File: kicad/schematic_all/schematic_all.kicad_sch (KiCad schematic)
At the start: 40 parts, among them J1 Power In, SW1 Button 1, SW2 Encoder 1, SW3 Button 2, SW4 Encoder 2, SW5 Button 3, U1 L7805, U2 RPi_Pico, U3 RDA5807M_Module, U4 LM386

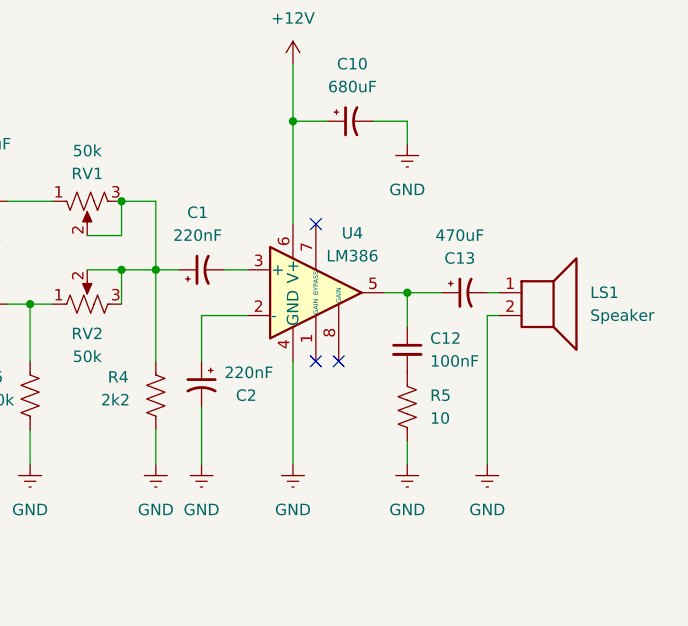
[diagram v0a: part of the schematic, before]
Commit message: Minor changes & Added additional testpoints
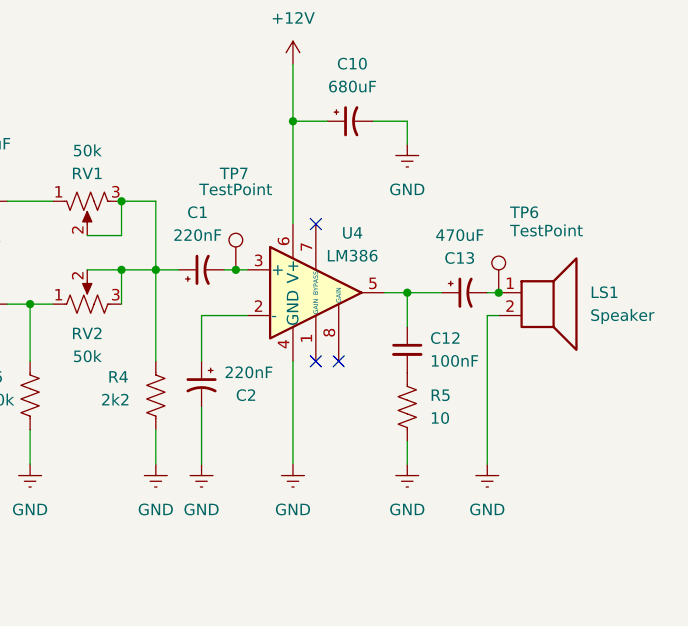
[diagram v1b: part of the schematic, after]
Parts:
- added TP6, TP7: TestPoint, Connector_PinHeader_2.54mm:PinHeader_1x01_P2.54mm_Vertical, symbol Connector:TestPoint
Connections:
- net at C1.2, U4.3 (+): now also TP7.1
- net at C13.2, LS1.1: now also TP6.1
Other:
- company: (none) -> Thomas Cool & Andrew Fischer
- title: (none) -> ECE 299 - Alarm Clock Radio
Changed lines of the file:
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@@
 	(generator_version "8.0")
 	(paper "A4")
+	(title_block
+		(title "ECE 299 - Alarm Clock Radio")
+		(date "2024-05-21")
+		(rev "6")
+		(company "Thomas Cool & Andrew Fischer")
+	)
 	(junction
 		(at 31.75 72.39)
@@
 	)
 	(junction
+		(at 261.62 129.54)
+		(diameter 0)
+		(color 0 0 0 0)
+	)
+	(junction
 		(at 77.47 63.5)
 		(diameter 0)
@@
 		(color 0 0 0 0)
 	)
+	(junction
+		(at 232.41 127)
+		(diameter 0)
+		(color 0 0 0 0)
+	)
 	(no_connect
 		(at 132.08 86.36)
@@
 	(wire
 		(pts
-			(xy 231.14 127) (xy 233.68 127)
+			(xy 231.14 127) (xy 232.41 127)
 		)
 		(stroke
@@
 	(wire
 		(pts
+			(xy 260.35 132.08) (xy 260.35 148.59)
+		)
+		(stroke
+			(width 0)
+			(type default)
+		)
+	)
+	(wire
+		(pts
 			(xy 41.91 69.85) (xy 41.91 72.39)
 		)
@@
 	(wire
 		(pts
+			(xy 232.41 127) (xy 233.68 127)
+		)
+		(stroke
+			(width 0)
+			(type default)
+		)
+	)
+	(wire
+		(pts
 			(xy 53.34 119.38) (xy 59.69 119.38)
 		)
@@
 	(wire
 		(pts
-			(xy 260.35 148.59) (xy 260.35 132.08)
-		)
-		(stroke
-			(width 0)
-			(type default)
-		)
-	)
-	(wire
-		(pts
 			(xy 248.92 129.54) (xy 251.46 129.54)
 		)
@@
 	)
 	(symbol
+		(lib_id "Connector:TestPoint")
+		(at 261.62 129.54 0)
+		(unit 1)
+		(exclude_from_sim no)
+		(in_bom yes)
+		(on_board yes)
+		(dnp no)
+		(property "Reference" "TP6"
+			(at 262.89 120.65 0)
+			(effects
+				(font
+					(size 1.27 1.27)
+				)
+				(justify left)
+			)
+		)
+		(property "Value" "TestPoint"
+			(at 262.89 122.682 0)
+			(effects
+				(font
+					(size 1.27 1.27)
+				)
+				(justify left)
+			)
+		)
+		(property "Footprint" "Connector_PinHeader_2.54mm:PinHeader_1x01_P2.54mm_Vertical"
+			(at 266.7 129.54 0)
+			(effects
+				(font
+					(size 1.27 1.27)
+				)
+				(hide yes)
+			)
+		)
+		(property "Datasheet" "~"
+			(at 266.7 129.54 0)
+			(effects
+				(font
+					(size 1.27 1.27)
+				)
+				(hide yes)
+			)
+		)
+		(property "Description" "test point"
+			(at 261.62 129.54 0)
+			(effects
+				(font
+					(size 1.27 1.27)
+				)
+				(hide yes)
+			)
+		)
+		(pin "1"
+		)
+		(instances
+			(project "schematic_all"
+				(path "/017a32bd-a431-4565-87b4-2161296abf15"
+					(reference "TP6")
+					(unit 1)
+				)
+			)
+		)
+	)
+	(symbol
 		(lib_id "power:+12V")
 		(at 29.21 20.32 0)
@@
 					(unit 1)
 				)
+			)
+		)
+	)
+	(symbol
+		(lib_id "Connector:TestPoint")
+		(at 232.41 127 0)
+		(unit 1)
+		(exclude_from_sim no)
+		(in_bom yes)
+		(on_board yes)
+		(dnp no)
+		(property "Reference" "TP7"
+			(at 230.632 116.332 0)
+			(effects
+				(font
+					(size 1.27 1.27)
+				)
+				(justify left)
+			)
+		)
+		(property "Value" "TestPoint"
+			(at 228.346 118.11 0)
+			(effects
+				(font
+					(size 1.27 1.27)
+				)
+				(justify left)
+			)
+		)
+		(property "Footprint" "Connector_PinHeader_2.54mm:PinHeader_1x01_P2.54mm_Vertical"
+			(at 237.49 127 0)
+			(effects
+				(font
+					(size 1.27 1.27)
+				)
+				(hide yes)
+			)
+		)
+		(property "Datasheet" "~"
+			(at 237.49 127 0)
+			(effects
+				(font
+					(size 1.27 1.27)
+				)
+				(hide yes)
+			)
+		)
+		(property "Description" "test point"
+			(at 232.41 127 0)
+			(effects
+				(font
+					(size 1.27 1.27)
+				)
+				(hide yes)
+			)
+		)
+		(pin "1"
+		)
+		(instances
+			(project "schematic_all"
+				(path "/017a32bd-a431-4565-87b4-2161296abf15"
+					(reference "TP7")
+					(unit 1)
+				)

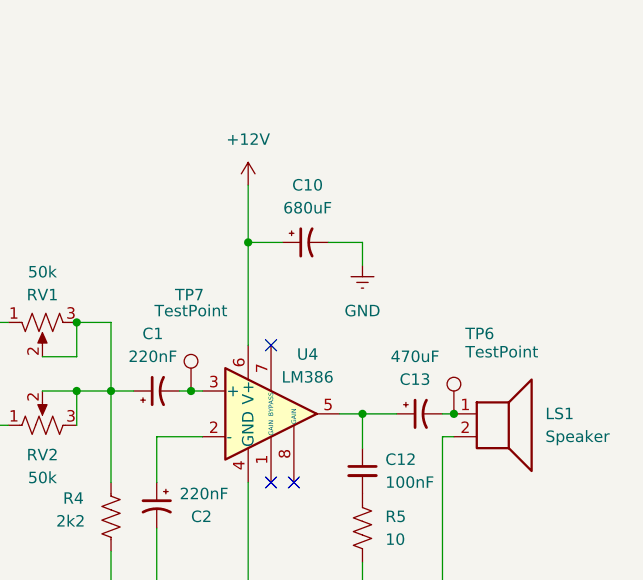
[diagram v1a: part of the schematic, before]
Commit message: adjustments on test points and ink
move speaker test point to before capacitor
increase size of designed by text
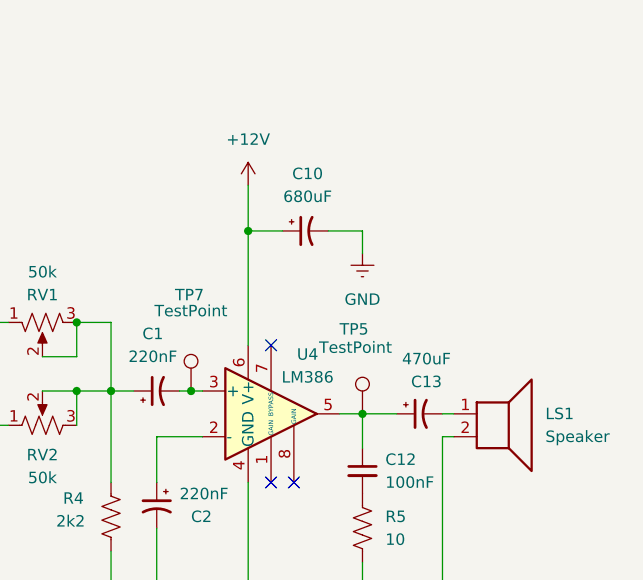
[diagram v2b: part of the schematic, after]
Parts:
- removed TP6: TestPoint, Connector_PinHeader_2.54mm:PinHeader_1x01_P2.54mm_Vertical, symbol Connector:TestPoint
- added TP5: TestPoint, Connector_PinHeader_2.54mm:PinHeader_1x01_P2.54mm_Vertical, symbol Connector:TestPoint
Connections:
- net at C12.1, C13.1, U4.5: now also TP5.1
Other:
- moved on the sheet: C10
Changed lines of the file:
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@@
 	)
 	(junction
-		(at 170.18 66.04)
+		(at 238.76 109.22)
 		(diameter 0)
 		(color 0 0 0 0)
 	)
 	(junction
-		(at 110.49 93.98)
+		(at 170.18 66.04)
 		(diameter 0)
 		(color 0 0 0 0)
 	)
 	(junction
-		(at 41.91 60.96)
+		(at 110.49 93.98)
 		(diameter 0)
 		(color 0 0 0 0)
 	)
 	(junction
-		(at 219.71 119.38)
+		(at 41.91 60.96)
 		(diameter 0)
 		(color 0 0 0 0)
 	)
 	(junction
-		(at 261.62 129.54)
+		(at 219.71 119.38)
 		(diameter 0)
 		(color 0 0 0 0)
@@
 	)
 	(junction
-		(at 238.76 110.49)
-		(diameter 0)
-		(color 0 0 0 0)
-	)
-	(junction
 		(at 120.65 93.98)
 		(diameter 0)
@@
 	(wire
 		(pts
-			(xy 251.46 110.49) (xy 251.46 113.03)
+			(xy 251.46 109.22) (xy 251.46 111.76)
 		)
 		(stroke
@@
 	(wire
 		(pts
-			(xy 247.65 110.49) (xy 251.46 110.49)
+			(xy 247.65 109.22) (xy 251.46 109.22)
 		)
 		(stroke
@@
 	(wire
 		(pts
-			(xy 238.76 110.49) (xy 242.57 110.49)
+			(xy 238.76 109.22) (xy 242.57 109.22)
 		)
 		(stroke
@@
 	(wire
 		(pts
-			(xy 238.76 110.49) (xy 238.76 121.92)
-		)
-		(stroke
-			(width 0)
-			(type default)
-		)
-	)
-	(wire
-		(pts
 			(xy 236.22 58.42) (xy 246.38 58.42)
 		)
@@
 	(wire
 		(pts
-			(xy 238.76 104.14) (xy 238.76 110.49)
+			(xy 238.76 104.14) (xy 238.76 109.22)
 		)
 		(stroke
@@
 	(wire
 		(pts
+			(xy 238.76 109.22) (xy 238.76 121.92)
+		)
+		(stroke
+			(width 0)
+			(type default)
+		)
+	)
+	(wire
+		(pts
 			(xy 86.36 121.92) (xy 86.36 111.76)
 		)
@@
 	)
 	(symbol
-		(lib_id "Connector:TestPoint")
-		(at 261.62 129.54 0)
-		(unit 1)
-		(exclude_from_sim no)
-		(in_bom yes)
-		(on_board yes)
-		(dnp no)
-		(property "Reference" "TP6"
-			(at 262.89 120.65 0)
-			(effects
-				(font
-					(size 1.27 1.27)
-				)
-				(justify left)
-			)
-		)
-		(property "Value" "TestPoint"
-			(at 262.89 122.682 0)
-			(effects
-				(font
-					(size 1.27 1.27)
-				)
-				(justify left)
-			)
-		)
-		(property "Footprint" "Connector_PinHeader_2.54mm:PinHeader_1x01_P2.54mm_Vertical"
-			(at 266.7 129.54 0)
-			(effects
-				(font
-					(size 1.27 1.27)
-				)
-				(hide yes)
-			)
-		)
-		(property "Datasheet" "~"
-			(at 266.7 129.54 0)
-			(effects
-				(font
-					(size 1.27 1.27)
-				)
-				(hide yes)
-			)
-		)
-		(property "Description" "test point"
-			(at 261.62 129.54 0)
-			(effects
-				(font
-					(size 1.27 1.27)
-				)
-				(hide yes)
-			)
-		)
-		(pin "1"
-		)
-		(instances
-			(project "schematic_all"
-				(path "/017a32bd-a431-4565-87b4-2161296abf15"
-					(reference "TP6")
-					(unit 1)
-				)
-			)
-		)
-	)
-	(symbol
 		(lib_id "power:+12V")
 		(at 29.21 20.32 0)
@@
 	(symbol
 		(lib_id "Device:C_Polarized_Small_US")
-		(at 245.11 110.49 90)
+		(at 245.11 109.22 90)
 		(mirror x)
 		(unit 1)
@@
 		(dnp no)
 		(property "Reference" "C10"
-			(at 245.364 104.14 90)
+			(at 245.364 102.87 90)
 			(effects
 				(font
@@
 		)
 		(property "Value" "680uF"
-			(at 245.364 106.68 90)
+			(at 245.364 105.41 90)
 			(effects
 				(font
@@
 		)
 		(property "Footprint" "Capacitor_THT:CP_Radial_D8.0mm_P3.50mm"
-			(at 245.11 110.49 0)
+			(at 245.11 109.22 0)
 			(effects
 				(font
@@
 		)
 		(property "Datasheet" "~"
-			(at 245.11 110.49 0)
+			(at 245.11 109.22 0)
 			(effects
 				(font
@@
 		)
 		(property "Description" "Polarized capacitor, small US symbol"
-			(at 245.11 110.49 0)
+			(at 245.11 109.22 0)
 			(effects
 				(font
@@
 	(symbol
 		(lib_id "power:Earth")
-		(at 251.46 113.03 0)
+		(at 251.46 111.76 0)
 		(mirror y)
 		(unit 1)
@@
 		(fields_autoplaced yes)
 		(property "Reference" "#PWR029"
-			(at 251.46 119.38 0)
+			(at 251.46 118.11 0)
 			(effects
 				(font
@@
 		)
 		(property "Value" "GND"
-			(at 251.46 118.11 0)
+			(at 251.46 116.84 0)
 			(effects
 				(font
@@
 		)
 		(property "Footprint" ""
-			(at 251.46 113.03 0)
+			(at 251.46 111.76 0)
 			(effects
 				(font
@@
 		)
 		(property "Datasheet" "~"
-			(at 251.46 113.03 0)
+			(at 251.46 111.76 0)
 			(effects
 				(font
@@
 		)
 		(property "Description" "Power symbol creates a global label with name \"Earth\""
-			(at 251.46 113.03 0)
+			(at 251.46 111.76 0)
 			(effects
 				(font
@@
 		(dnp no)
 		(property "Reference" "C13"
-			(at 257.302 125.73 90)
+			(at 258.572 125.984 90)
 			(effects
 				(font
@@
 		)
 		(property "Value" "470uF"
-			(at 257.302 123.19 90)
+			(at 258.572 123.444 90)
 			(effects
 				(font
@@
 					(unit 1)
 				)
+			)
+		)
+	)
+	(symbol
+		(lib_id "Connector:TestPoint")
+		(at 251.46 129.54 0)
+		(unit 1)
+		(exclude_from_sim no)
+		(in_bom yes)
+		(on_board yes)
+		(dnp no)
+		(property "Reference" "TP5"
+			(at 248.92 120.142 0)
+			(effects
+				(font
+					(size 1.27 1.27)
+				)
+				(justify left)
+			)
+		)
+		(property "Value" "TestPoint"
+			(at 246.634 122.174 0)
+			(effects
+				(font
+					(size 1.27 1.27)
+				)
+				(justify left)
+			)
+		)
+		(property "Footprint" "Connector_PinHeader_2.54mm:PinHeader_1x01_P2.54mm_Vertical"
+			(at 256.54 129.54 0)
+			(effects
+				(font
+					(size 1.27 1.27)
+				)
+				(hide yes)
+			)
+		)
+		(property "Datasheet" "~"
+			(at 256.54 129.54 0)
+			(effects
+				(font
+					(size 1.27 1.27)
+				)
+				(hide yes)
+			)
+		)
+		(property "Description" "test point"
+			(at 251.46 129.54 0)
+			(effects
+				(font
+					(size 1.27 1.27)
+				)
+				(hide yes)
+			)
+		)
+		(pin "1"
+		)
+		(instances
+			(project "schematic_all"
+				(path "/017a32bd-a431-4565-87b4-2161296abf15"
+					(reference "TP5")
+					(unit 1)
+				)

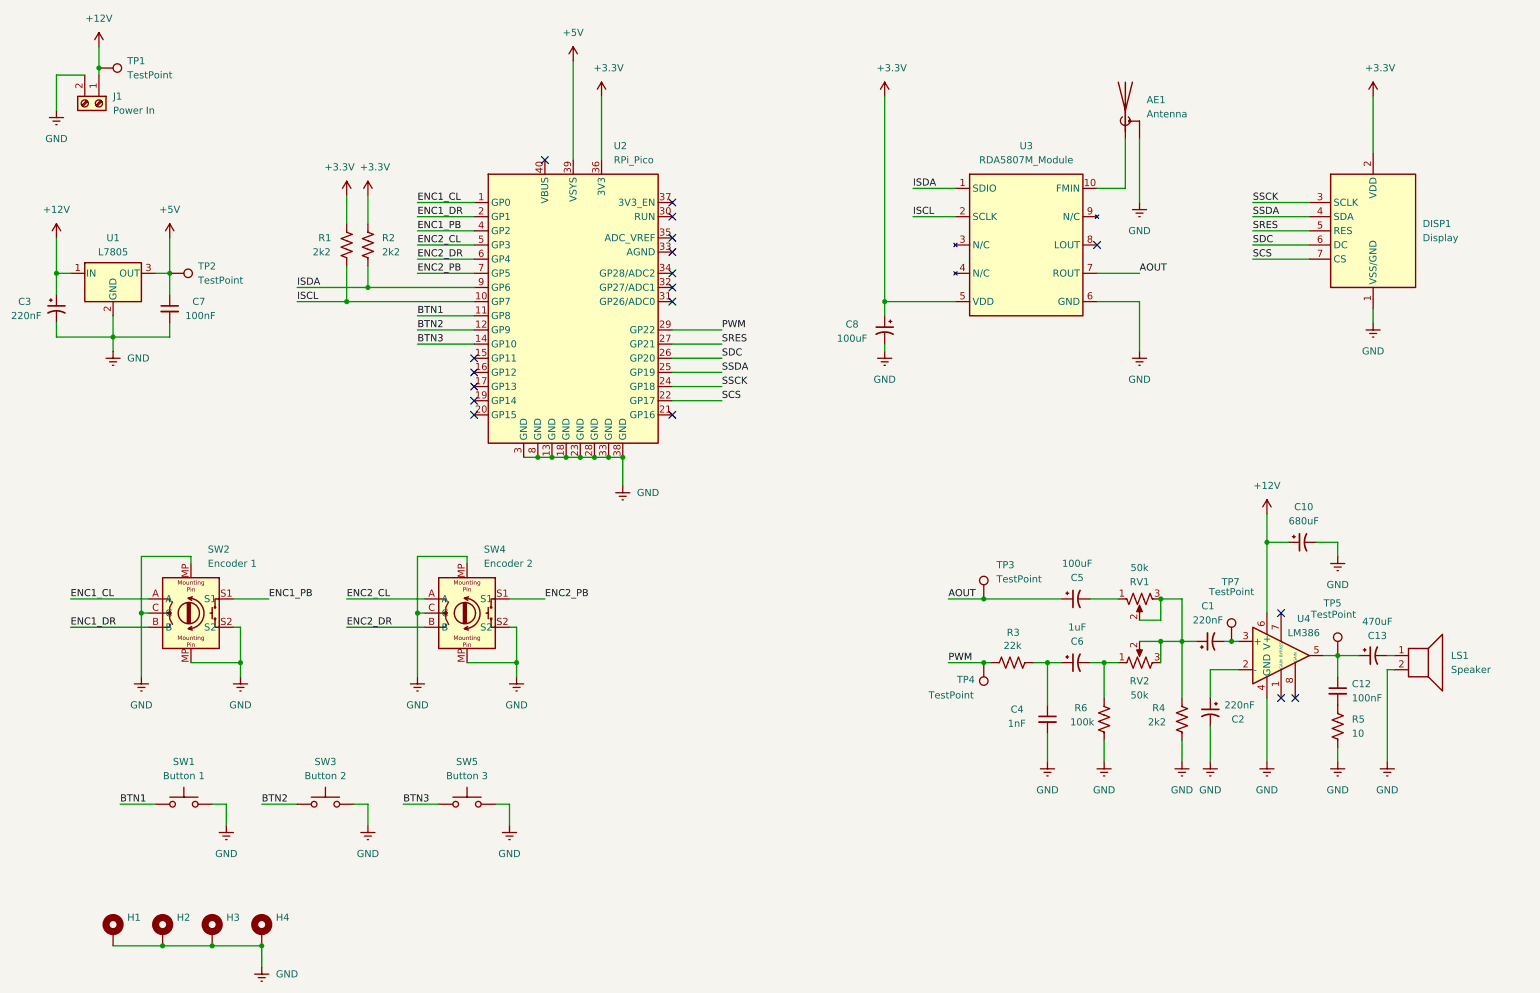
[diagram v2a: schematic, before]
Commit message: full board check
replace incorrect radial cap with disc
change capacitor values around amp
add jack labels
reground pot chassis
tweak positions
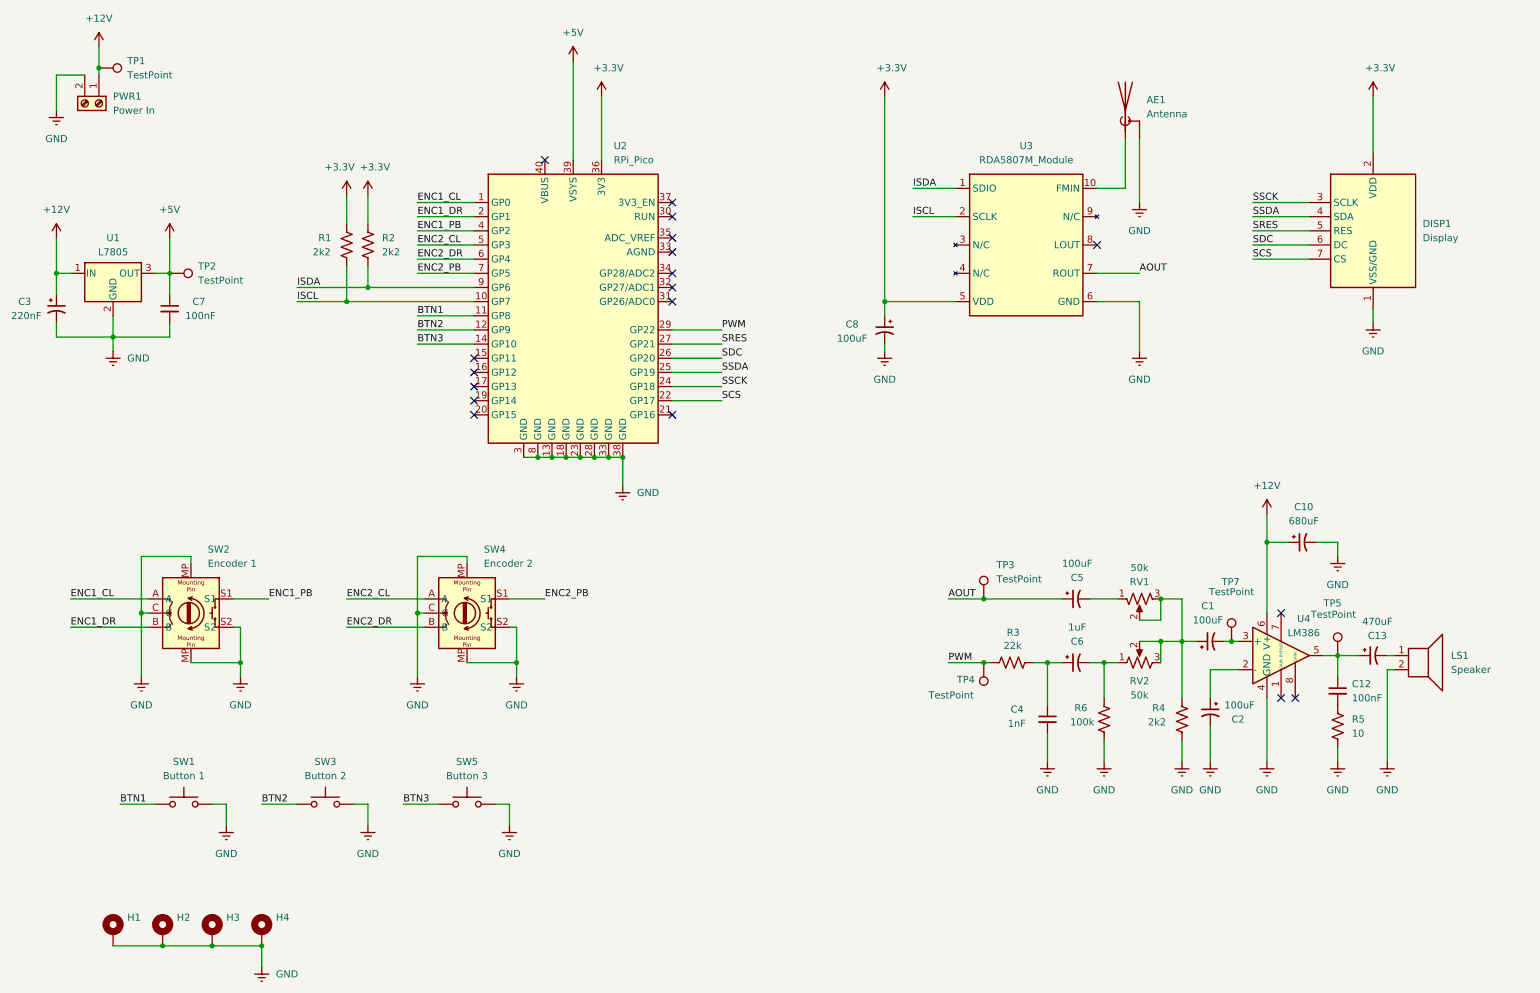
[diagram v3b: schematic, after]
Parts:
- C1, C2: value 220nF -> 100uF
- C4: footprint Capacitor_THT:CP_Radial_D5.0mm_P2.00mm -> Capacitor_THT:C_Disc_D5.0mm_W2.5mm_P5.00mm
- renumbered J1 to PWR1
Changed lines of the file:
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@@
 		(title "ECE 299 - Alarm Clock Radio")
 		(date "2024-05-21")
-		(rev "6")
+		(rev "2.7")
 		(company "Thomas Cool & Andrew Fischer")
 	)
@@
 			)
 		)
-		(property "Value" "220nF"
+		(property "Value" "100uF"
 			(at 228.1682 123.19 90)
 			(effects
@@
 		(dnp no)
 		(fields_autoplaced yes)
-		(property "Reference" "J1"
+		(property "Reference" "PWR1"
 			(at 31.75 29.2099 90)
 			(effects
@@
 			(project ""
 				(path "/017a32bd-a431-4565-87b4-2161296abf15"
-					(reference "J1")
+					(reference "PWR1")
 					(unit 1)
 				)
@@
 			)
 		)
-		(property "Value" "220nF"
+		(property "Value" "100uF"
 			(at 231.14 138.4365 0)
 			(effects
@@
 			)
 		)
-		(property "Footprint" "Capacitor_THT:CP_Radial_D5.0mm_P2.00mm"
+		(property "Footprint" "Capacitor_THT:C_Disc_D5.0mm_W2.5mm_P5.00mm"
 			(at 199.39 140.97 0)
 			(effects
